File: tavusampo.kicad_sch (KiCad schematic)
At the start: 1 part, among them U1 Z80CPU

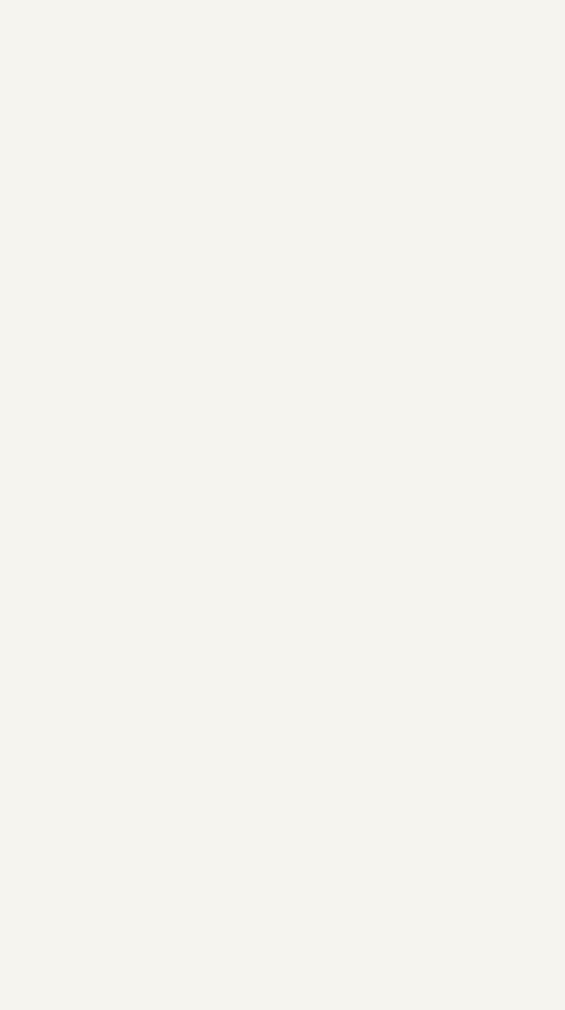
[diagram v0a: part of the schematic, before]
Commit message: Added RAM and ROM
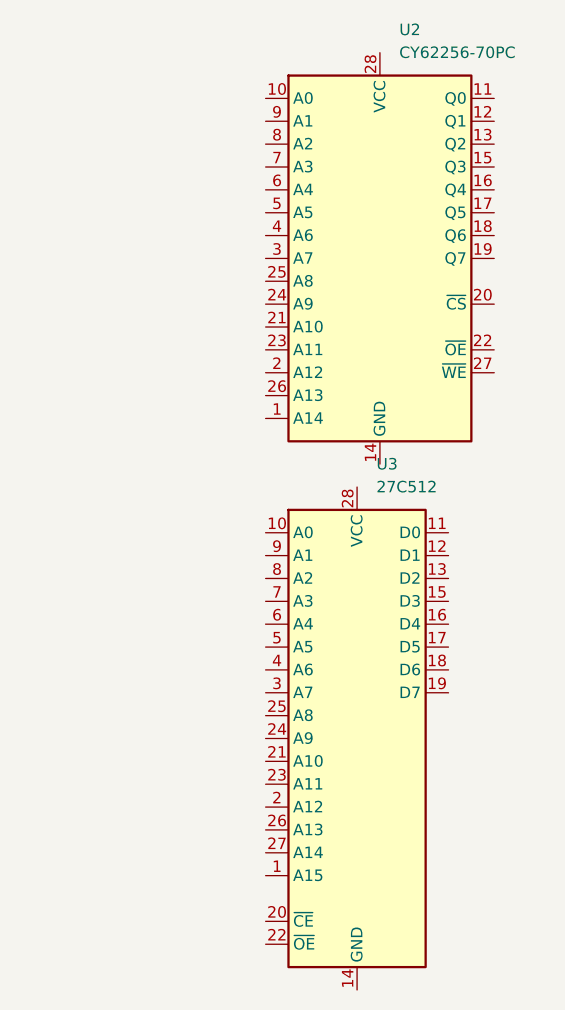
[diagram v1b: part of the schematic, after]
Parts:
- added U2: CY62256-70PC, Package_DIP:DIP-28_W15.24mm, symbol Memory_RAM:CY62256-70PC
- added U3: 27C512, Package_DIP:DIP-28_W15.24mm, symbol Memory_EPROM:27C512
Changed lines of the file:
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@@
+		)
+	)
+	(symbol
+		(lib_id "Memory_RAM:CY62256-70PC")
+		(at 241.3 81.28 0)
+		(unit 1)
+		(exclude_from_sim no)
+		(in_bom yes)
+		(on_board yes)
+		(dnp no)
+		(fields_autoplaced yes)
+		(property "Reference" "U2"
+			(at 243.4433 55.88 0)
+			(effects
+				(font
+					(size 1.27 1.27)
+				)
+				(justify left)
+			)
+		)
+		(property "Value" "CY62256-70PC"
+			(at 243.4433 58.42 0)
+			(effects
+				(font
+					(size 1.27 1.27)
+				)
+				(justify left)
+			)
+		)
+		(property "Footprint" "Package_DIP:DIP-28_W15.24mm"
+			(at 241.3 83.82 0)
+			(effects
+				(font
+					(size 1.27 1.27)
+				)
+				(hide yes)
+			)
+		)
+		(property "Datasheet" "https://ecee.colorado.edu/~mcclurel/Cypress_SRAM_CY62256.pdf"
+			(at 241.3 83.82 0)
+			(effects
+				(font
+					(size 1.27 1.27)
+				)
+				(hide yes)
+			)
+		)
+		(property "Description" "256K (32K x 8) Static RAM, 70ns, DIP-28"
+			(at 241.3 81.28 0)
+			(effects
+				(font
+					(size 1.27 1.27)
+				)
+				(hide yes)
+			)
+		)
+		(pin "7"
+		)
+		(pin "6"
+		)
+		(pin "8"
+		)
+		(pin "9"
+		)
+		(pin "10"
+		)
+		(pin "22"
+		)
+		(pin "26"
+		)
+		(pin "17"
+		)
+		(pin "16"
+		)
+		(pin "14"
+		)
+		(pin "4"
+		)
+		(pin "12"
+		)
+		(pin "25"
+		)
+		(pin "3"
+		)
+		(pin "5"
+		)
+		(pin "2"
+		)
+		(pin "23"
+		)
+		(pin "21"
+		)
+		(pin "24"
+		)
+		(pin "19"
+		)
+		(pin "20"
+		)
+		(pin "27"
+		)
+		(pin "15"
+		)
+		(pin "13"
+		)
+		(pin "18"
+		)
+		(pin "11"
+		)
+		(pin "28"
+		)
+		(pin "1"
+		)
+		(instances
+			(project ""
+				(path "/81bcdf73-d761-4ea2-901c-14ff009a9c37"
+					(reference "U2")
+					(unit 1)
+				)
+			)
+		)
+	)
+	(symbol
+		(lib_id "Memory_EPROM:27C512")
+		(at 238.76 134.62 0)
+		(unit 1)
+		(exclude_from_sim no)
+		(in_bom yes)
+		(on_board yes)
+		(dnp no)
+		(fields_autoplaced yes)
+		(property "Reference" "U3"
+			(at 240.9033 104.14 0)
+			(effects
+				(font
+					(size 1.27 1.27)
+				)
+				(justify left)
+			)
+		)
+		(property "Value" "27C512"
+			(at 240.9033 106.68 0)
+			(effects
+				(font
+					(size 1.27 1.27)
+				)
+				(justify left)
+			)
+		)
+		(property "Footprint" "Package_DIP:DIP-28_W15.24mm"
+			(at 238.76 134.62 0)
+			(effects
+				(font
+					(size 1.27 1.27)
+				)
+				(hide yes)
+			)
+		)
+		(property "Datasheet" "http://ww1.microchip.com/downloads/en/DeviceDoc/doc0015.pdf"
+			(at 238.76 134.62 0)
+			(effects
+				(font
+					(size 1.27 1.27)
+				)
+				(hide yes)
+			)
+		)
+		(property "Description" "OTP EPROM 512 KiBit"
+			(at 238.76 134.62 0)
+			(effects
+				(font
+					(size 1.27 1.27)
+				)
+				(hide yes)
+			)
+		)
+		(pin "26"
+		)
+		(pin "15"
+		)
+		(pin "21"
+		)
+		(pin "1"
+		)
+		(pin "2"
+		)
+		(pin "27"
+		)
+		(pin "22"
+		)
+		(pin "9"
+		)
+		(pin "19"
+		)
+		(pin "7"
+		)
+		(pin "20"
+		)
+		(pin "10"
+		)
+		(pin "14"
+		)
+		(pin "8"
+		)
+		(pin "6"
+		)
+		(pin "23"
+		)
+		(pin "3"
+		)
+		(pin "5"
+		)
+		(pin "4"
+		)
+		(pin "25"
+		)
+		(pin "17"
+		)
+		(pin "11"
+		)
+		(pin "18"
+		)
+		(pin "16"
+		)
+		(pin "13"
+		)
+		(pin "24"
+		)
+		(pin "12"
+		)
+		(pin "28"
+		)
+		(instances
+			(project ""
+				(path "/81bcdf73-d761-4ea2-901c-14ff009a9c37"
+					(reference "U3")
+					(unit 1)
+				)
+			)
 		)
 	)

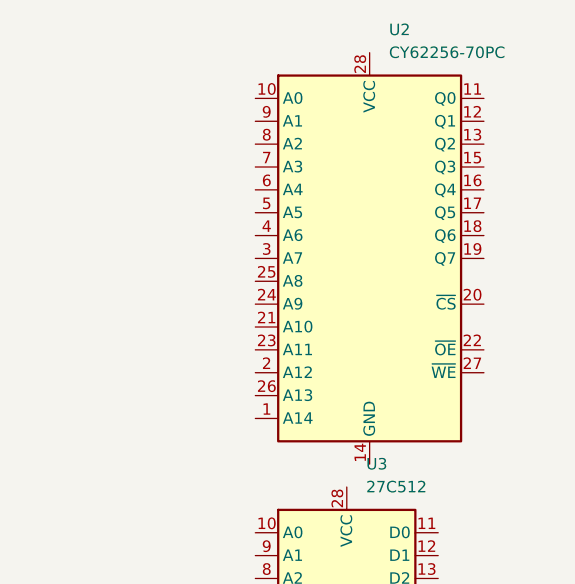
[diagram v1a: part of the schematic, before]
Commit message: Fixed RAM pins
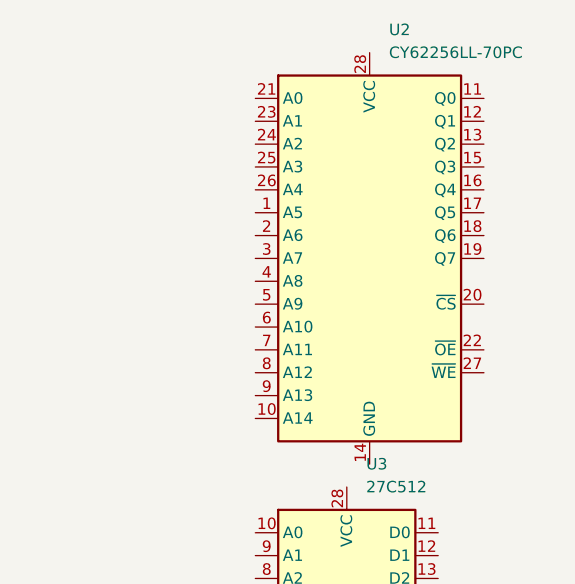
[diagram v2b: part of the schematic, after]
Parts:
- U2: value CY62256-70PC -> CY62256LL-70PC
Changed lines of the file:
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@@
 			)
 		)
-		(property "Value" "CY62256-70PC"
+		(property "Value" "CY62256LL-70PC"
 			(at 243.4433 58.42 0)
 			(effects

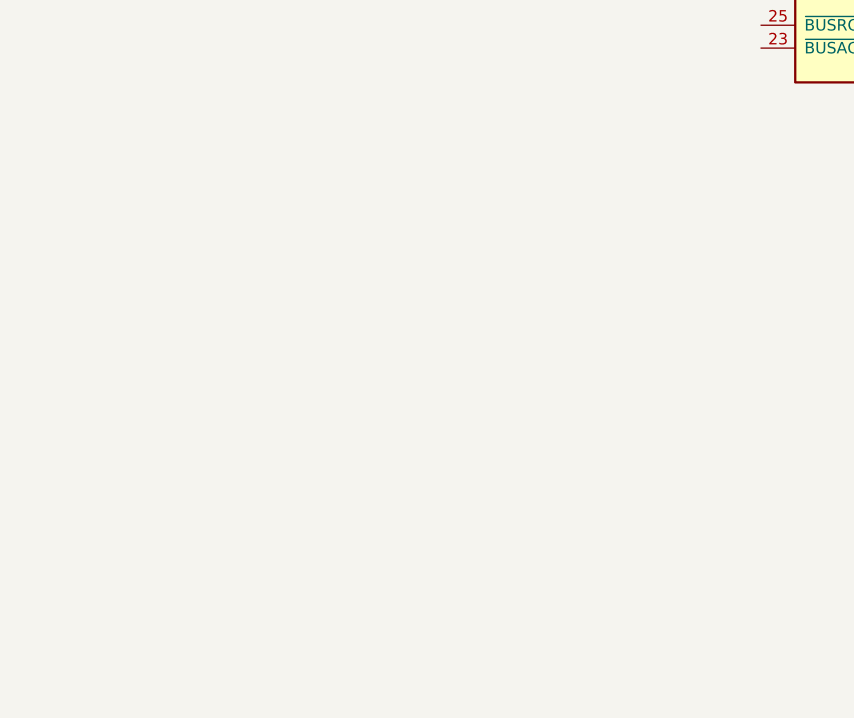
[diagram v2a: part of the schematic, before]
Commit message: added some displays
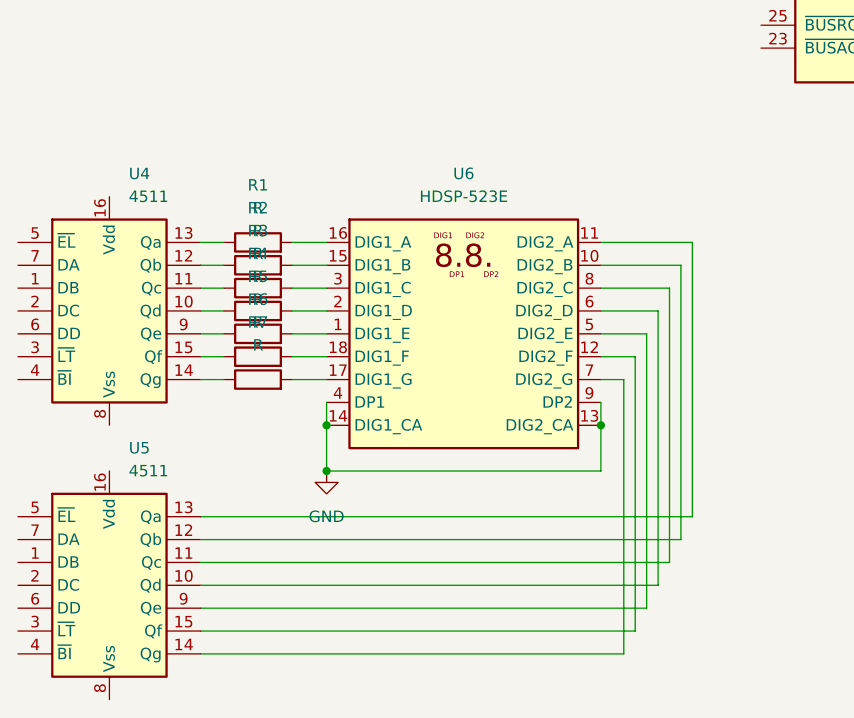
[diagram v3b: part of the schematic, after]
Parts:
- added R1, R2, R3, R4, R5, R6, R7: R, symbol Device:R
- added U4, U5: 4511, symbol 4xxx_IEEE:4511
- added U6: HDSP-523E, Display_7Segment:DA56-11SURKWA, symbol Display_Character:DA56-11SURKWA
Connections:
- new net: U5.10 (Qd), U6.6 (DIG2_D)
- new net: U5.11 (Qc), U6.8 (DIG2_C)
- new net: U5.12 (Qb), U6.10 (DIG2_B)
- new net: U5.13 (Qa), U6.11 (DIG2_A)
- new net: U5.14 (Qg), U6.7 (DIG2_G)
- new net: U5.15 (Qf), U6.12 (DIG2_F)
- new net: U5.9 (Qe), U6.5 (DIG2_E)
- new net: R4.1, U4.10 (Qd)
- new net: R3.1, U4.11 (Qc)
- new net: R2.1, U4.12 (Qb)
- new net: R1.1, U4.13 (Qa)
- new net: R7.1, U4.14 (Qg)
- new net: R6.1, U4.15 (Qf)
- new net: R5.1, U4.9 (Qe)
- new net: R5.2, U6.1 (DIG1_E)
- new net: R2.2, U6.15 (DIG1_B)
- new net: R1.2, U6.16 (DIG1_A)
- new net: R7.2, U6.17 (DIG1_G)
- new net: R6.2, U6.18 (DIG1_F)
- new net: R4.2, U6.2 (DIG1_D)
- new net: R3.2, U6.3 (DIG1_C)
- new net GND: U6.13 (DIG2_CA), U6.14 (DIG1_CA), U6.4 (DP1), U6.9 (DP2)

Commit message: small update
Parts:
- added U7: SST39SF040, symbol Memory_Flash:SST39SF040
- added U8: AS6C4008-55PCN, Package_DIP:DIP-32_W15.24mm, symbol Memory_RAM:AS6C4008-55PCN
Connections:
- net GND: now also U1.29 (GND)
- net A11: now reaches U1.1 (A11)
- net D6: now reaches U1.10 (D6)
- net D6: now also U7.20 (D6), U8.20 (DQ6)
- net D2: now reaches U1.12 (D2)
- net D2: now also U7.15 (D2), U8.15 (DQ2)
- net D7: now reaches U1.13 (D7)
- net D7: now also U7.21 (D7), U8.21 (DQ7)
- net D0: now reaches U1.14 (D0)
- net D0: now also U7.13 (D0), U8.13 (DQ0)
- net D1: now reaches U1.15 (D1)
- net D1: now also U7.14 (D1), U8.14 (DQ1)
- net A12: now reaches U1.2 (A12)
- net RESET: now reaches U1.26 (~{RESET})
- net A13: now reaches U1.3 (A13)
- net A0: now reaches U1.30 (A0)
- net A1: now reaches U1.31 (A1)
- net A2: now reaches U1.32 (A2)
- net A3: now reaches U1.33 (A3)
- net A4: now reaches U1.34 (A4)
- net A5: now reaches U1.35 (A5)
- net A6: now reaches U1.36 (A6)
- net A7: now reaches U1.37 (A7)
- net A8: now reaches U1.38 (A8)
- net A9: now reaches U1.39 (A9)
- net A14: now reaches U1.4 (A14)
- net A10: now reaches U1.40 (A10)
- net A15: now reaches U1.5 (A15)
- net CLK: now reaches U1.6 (~{CLK})
- net D4: now reaches U1.7 (D4)
- net D4: now also U7.18 (D4), U8.18 (DQ4)
- net D3: now reaches U1.8 (D3)
- net D3: now also U7.17 (D3), U8.17 (DQ3)
- net D5: now reaches U1.9 (D5)
- net D5: now also U7.19 (D5), U8.19 (DQ5)
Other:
- moved on the sheet: U2, U3
